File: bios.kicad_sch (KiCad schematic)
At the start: 39 parts, among them U1201 TMUX1574RSVR, U1202 MT25QU01GBBB8_SOIC, U1204 TMUX1574RSVR, U1205 MT25QU01GBBB8_SOIC

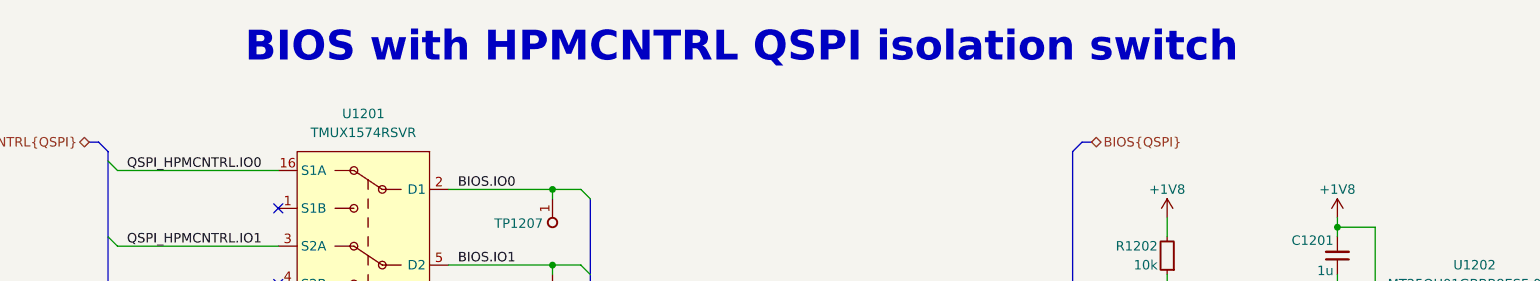
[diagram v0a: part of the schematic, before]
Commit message: [#100282] Add missing schematic sheet names and align them all
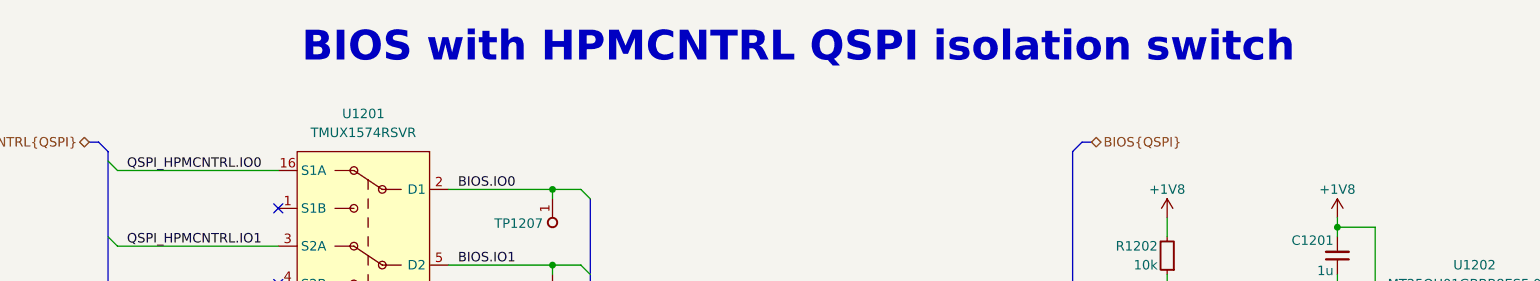
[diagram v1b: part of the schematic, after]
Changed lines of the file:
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@@
 	(text "BIOS with HPMCNTRL QSPI isolation switch\n"
 		(exclude_from_sim no)
-		(at 152.4 25.4 0)
+		(at 160.02 25.4 0)
 		(effects
 			(font

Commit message: [#100501] Reannotate schematic
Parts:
- renumbered C1201 to C87, C1202 to C88, C1203 to C89, C1204 to C90, R1202 to R114, R1210 to R115, R1207 to R116, R1211 to R117, R1214 to R118, R1215 to R119, R1216 to R120, R1217 to R121, R1204 to R122, R1208 to R123, R1206 to R124, R1224 to R125, R1205 to R126, R1220 to R127, R1221 to R128, R1222 to R129, R1223 to R130, R1209 to R131, R1203 to R132, R1212 to R133, R1225 to R134, R1201 to R135, R1213 to R136, TP1204 to TP10, TP1202 to TP11, TP1203 to TP12, TP1201 to TP13, TP1207 to TP6, TP1206 to TP7, TP1205 to TP8, TP1208 to TP9, U1201 to U13, U1202 to U14, U1204 to U15, U1205 to U16

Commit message: [#100501] Clean ERC
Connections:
- net ~{ISO_EN0} renamed ~{ISO_EN}
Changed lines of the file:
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@@
-		)
-	)
-	(label "~{ISO_EN0}"
-		(at 76.2 87.63 0)
-		(effects
-			(font
-				(size 1.27 1.27)
-			)
-			(justify left bottom)
 		)
 	)
@@
 		)
 	)
-	(label "~{ISO_EN1}"
+	(label "~{ISO_EN}"
 		(at 76.2 154.94 0)
 		(effects

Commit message: [#100501] Reannotate schematic
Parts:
- renumbered C87 to C91, C88 to C92, C89 to C93, C90 to C94, R114 to R148, R115 to R149, R116 to R150, R117 to R151, R118 to R152, R119 to R153, R120 to R154, R121 to R155, R122 to R156, R123 to R157, R124 to R158, R125 to R159, R126 to R160, R127 to R161, R128 to R162, R129 to R163, R130 to R164, R131 to R165, R132 to R166, R133 to R167, R134 to R168, R135 to R169, R136 to R170, TP6 to TP10, TP7 to TP11, TP8 to TP12, TP9 to TP13, TP10 to TP14, TP11 to TP15, TP12 to TP16, TP13 to TP17, U13 to U12, U14 to U13, U15 to U14, U16 to U15

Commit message: [#100501] Perform minor BOM consolidation
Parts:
- C91, C93: value C_1u_0402 -> C_1u_25V_0402; symbol antmicroCapacitors0402:C_1u_0402 -> antmicroCapacitors0402:C_1u_25V_0402; Dielectric (none) -> X5R; MPN C1005X6S1A105K050BC -> GRM155R61E105KE11J; Manufacturer TDK -> Murata; Voltage (none) -> 25V
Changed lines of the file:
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@@
 	)
 	(symbol
-		(lib_id "antmicroCapacitors0402:C_1u_0402")
+		(lib_id "antmicroCapacitors0402:C_1u_25V_0402")
 		(at 232.41 106.68 270)
 		(mirror x)
@@
 			)
 		)
-		(property "Value" "C_1u_0402"
+		(property "Value" "C_1u_25V_0402"
 			(at 222.25 86.36 0)
 			(hide yes)
@@
 			)
 		)
-		(property "Datasheet" "https://product.tdk.com/en/search/capacitor/ceramic/mlcc/info?part_no=C1005X6S1A105K050BC"
+		(property "Datasheet" "https://www.murata.com/products/productdetail?partno=GRM155R61E105KE11%23"
 			(at 217.17 86.36 0)
 			(hide yes)
@@
 			)
 		)
-		(property "Description" "SMD Multilayer Ceramic Capacitor, 1 µF, 10 V, 0402 [1005 Metric], ± 10%, X6S, C"
+		(property "Description" "SMD Multilayer Ceramic Capacitor, 1 µF, 25 V, 0402 [1005 Metric], ± 10%, X5R, GRM Series"
 			(at 199.39 86.36 0)
 			(hide yes)
@@
 			)
 		)
-		(property "MPN" "C1005X6S1A105K050BC"
+		(property "MPN" "GRM155R61E105KE11J"
 			(at 214.63 86.36 0)
 			(hide yes)
@@
 			)
 		)
-		(property "Manufacturer" "TDK"
+		(property "Manufacturer" "Murata"
 			(at 212.09 86.36 0)
 			(hide yes)
@@
 			)
 		)
-		(property "Voltage" ""
+		(property "Voltage" "25V"
 			(at 204.47 86.36 0)
 			(hide yes)
@@
 			)
 		)
-		(property "Dielectric" ""
+		(property "Dielectric" "X5R"
 			(at 201.93 86.36 0)
 			(hide yes)
@@
 	)
 	(symbol
-		(lib_id "antmicroCapacitors0402:C_1u_0402")
+		(lib_id "antmicroCapacitors0402:C_1u_25V_0402")
 		(at 232.41 55.88 270)
 		(mirror x)
@@
 			)
 		)
-		(property "Value" "C_1u_0402"
+		(property "Value" "C_1u_25V_0402"
 			(at 222.25 35.56 0)
 			(hide yes)
@@
 			)
 		)
-		(property "Datasheet" "https://product.tdk.com/en/search/capacitor/ceramic/mlcc/info?part_no=C1005X6S1A105K050BC"
+		(property "Datasheet" "https://www.murata.com/products/productdetail?partno=GRM155R61E105KE11%23"
 			(at 217.17 35.56 0)
 			(hide yes)
@@
 			)
 		)
-		(property "Description" "SMD Multilayer Ceramic Capacitor, 1 µF, 10 V, 0402 [1005 Metric], ± 10%, X6S, C"
+		(property "Description" "SMD Multilayer Ceramic Capacitor, 1 µF, 25 V, 0402 [1005 Metric], ± 10%, X5R, GRM Series"
 			(at 199.39 35.56 0)
 			(hide yes)
@@
 			)
 		)
-		(property "MPN" "C1005X6S1A105K050BC"
+		(property "MPN" "GRM155R61E105KE11J"
 			(at 214.63 35.56 0)
 			(hide yes)
@@
 			)
 		)
-		(property "Manufacturer" "TDK"
+		(property "Manufacturer" "Murata"
 			(at 212.09 35.56 0)
 			(hide yes)
@@
 			)
 		)
-		(property "Voltage" ""
+		(property "Voltage" "25V"
 			(at 204.47 35.56 0)
 			(hide yes)
@@
 			)
 		)
-		(property "Dielectric" ""
+		(property "Dielectric" "X5R"
 			(at 201.93 35.56 0)
 			(hide yes)
